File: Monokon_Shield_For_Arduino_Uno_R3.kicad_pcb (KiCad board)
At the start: 2 copper layers, 68.6 x 53.3 mm, 23 parts, among them CN1 2x5 10-Pin Male Box Header, CN2 2x5 10-Pin Male Box Header, CN3 6-Pin Headers, J1 locked, J2 Digital/PWM, J3 Analog, J4 Digital/PWM, Q1 2SC1815, Q2 2SC1815, Q3 2SC1815

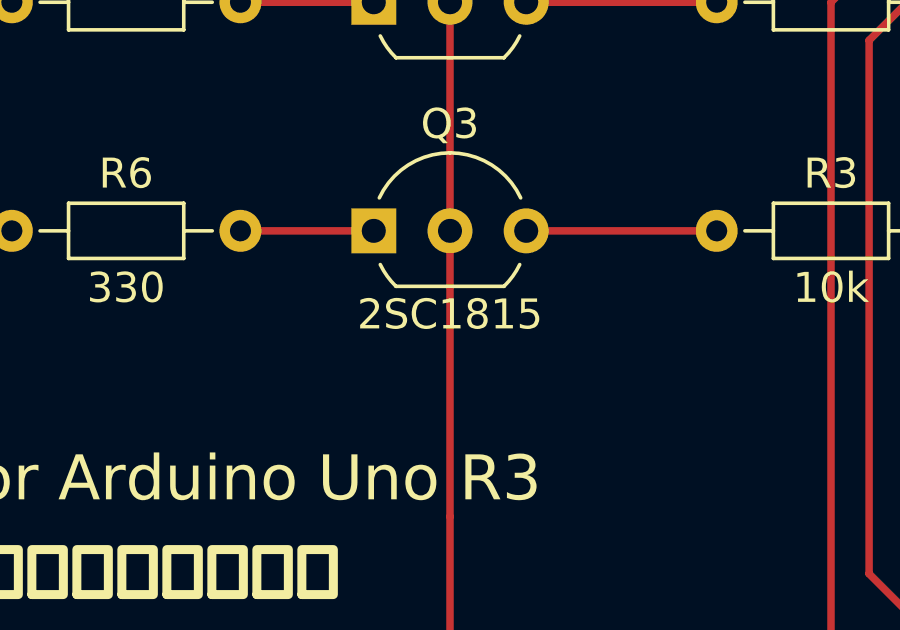
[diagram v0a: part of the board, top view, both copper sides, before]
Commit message: シルクの部品名を修正
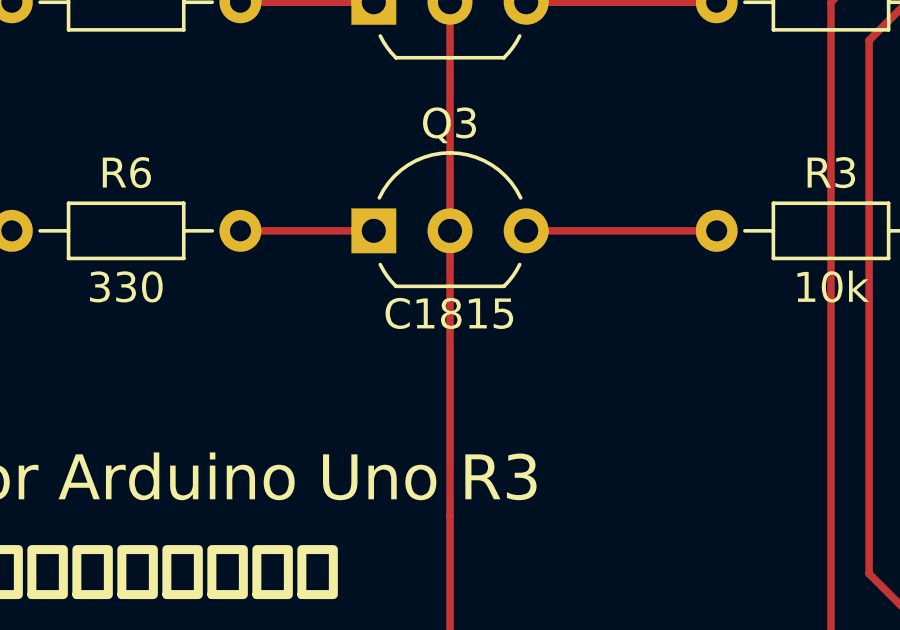
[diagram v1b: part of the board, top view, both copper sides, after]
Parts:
- Q1, Q2, Q3: value 2SC1815 -> C1815
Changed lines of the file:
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@@
       (effects (font (size 1 1) (thickness 0.15)))
     )
-    (fp_text value "2SC1815" (at 2.54 2.79) (layer "F.Fab")
+    (fp_text value "C1815" (at 2.54 2.79) (layer "F.Fab")
       (effects (font (size 1 1) (thickness 0.15)))
     )
@@
       (effects (font (size 1 1) (thickness 0.15)))
     )
-    (fp_text value "2SC1815" (at 2.54 2.79) (layer "F.SilkS")
+    (fp_text value "C1815" (at 2.54 2.79) (layer "F.SilkS")
       (effects (font (size 1 1) (thickness 0.15)))
     )
@@
       (effects (font (size 1 1) (thickness 0.15)))
     )
-    (fp_text value "2SC1815" (at 2.54 2.79) (layer "F.Fab")
-      (effects (font (size 1 1) (thickness 0.15)))
-    )
+    (fp_text value "C1815" (at 2.54 2.79) (layer "F.Fab")
+      (effects (font (size 1 1) (thickness 0.15)))
+    )
